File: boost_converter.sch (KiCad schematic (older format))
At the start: 9 parts, among them U4 TPS61236P

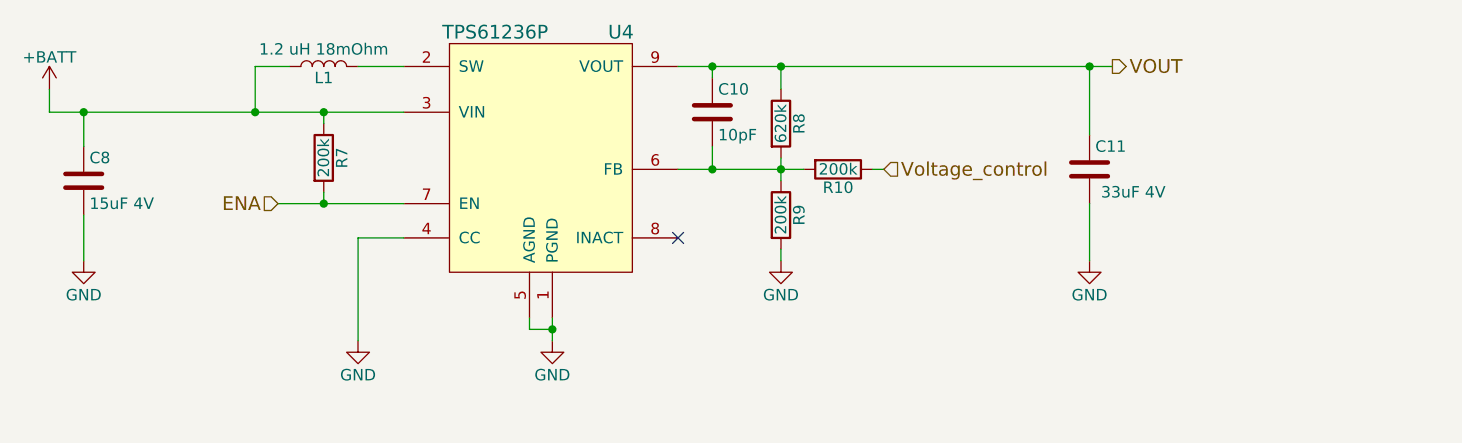
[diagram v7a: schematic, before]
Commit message: Changed pinout, added voltage and current reading
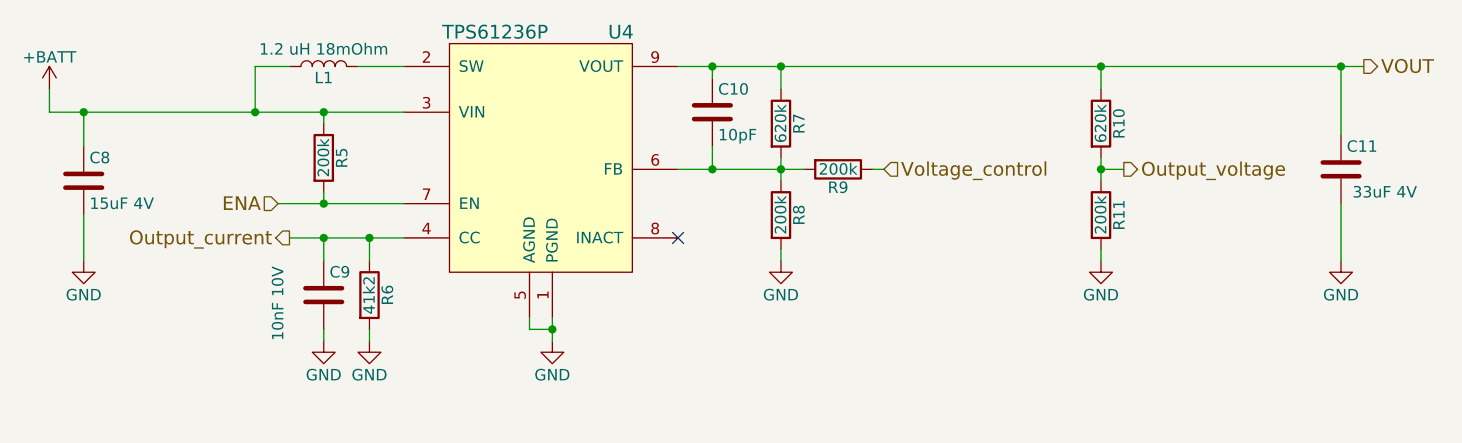
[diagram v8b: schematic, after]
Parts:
- added C9: 10nF 10V, Capacitors_SMD:C_0402, symbol C
- added R10: 620k, Resistors_SMD:R_0402, symbol R
- added R11: 200k, Resistors_SMD:R_0402, symbol R
- added R6: 41k2, Resistors_SMD:R_0402, symbol R
- C10: footprint (none) -> Capacitors_SMD:C_0402
- renumbered R7 to R5, R8 to R7, R9 to R8, R10 to R9
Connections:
- net GND: now also C9.2, R11.2, R6.2; no longer U4.4 (CC)
- net VOUT: now also R10.1
- new net Output_current: C9.1, R6.1, U4.4 (CC)
- new net Output_voltage: R10.2, R11.1
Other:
- moved on the sheet: C11
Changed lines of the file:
@@
 F 0 "C10" H 6575 3650 50  0000 L CNN
 F 1 "10pF" H 6575 3450 50  0000 L CNN
-F 2 "" H 6588 3400 50  0001 C CNN
+F 2 "Capacitors_SMD:C_0402" H 6588 3400 50  0001 C CNN
 F 3 "" H 6550 3550 50  0001 C CNN
 	1    6550 3550
@@
 $EndComp
 $Comp
-L R R8
+L R R7
 U 1 1 5AA40DAF
 P 6850 3600
-F 0 "R8" V 6930 3600 50  0000 C CNN
+F 0 "R7" V 6930 3600 50  0000 C CNN
 F 1 "620k" V 6850 3600 50  0000 C CNN
 F 2 "Resistors_SMD:R_0402" V 6780 3600 50  0001 C CNN
@@
 $EndComp
 $Comp
-L R R9
+L R R8
 U 1 1 5AA40DF4
 P 6850 4000
-F 0 "R9" V 6930 4000 50  0000 C CNN
+F 0 "R8" V 6930 4000 50  0000 C CNN
 F 1 "200k" V 6850 4000 50  0000 C CNN
 F 2 "Resistors_SMD:R_0402" V 6780 4000 50  0001 C CNN
@@
 $EndComp
 $Comp
-L GND #PWR032
+L GND #PWR37
 U 1 1 5AA40E28
 P 6850 4200
-F 0 "#PWR032" H 6850 3950 50  0001 C CNN
+F 0 "#PWR37" H 6850 3950 50  0001 C CNN
 F 1 "GND" H 6850 4050 50  0000 C CNN
 F 2 "" H 6850 4200 50  0001 C CNN
@@
 $EndComp
 $Comp
-L GND #PWR033
+L GND #PWR36
 U 1 1 5AA40E49
 P 5850 4550
-F 0 "#PWR033" H 5850 4300 50  0001 C CNN
+F 0 "#PWR36" H 5850 4300 50  0001 C CNN
 F 1 "GND" H 5850 4400 50  0000 C CNN
 F 2 "" H 5850 4550 50  0001 C CNN
@@
 L C C11
 U 1 1 5AA40FA0
-P 8200 3800
-F 0 "C11" H 8225 3900 50  0000 L CNN
-F 1 "33uF 4V" H 8250 3700 50  0000 L CNN
-F 2 "" H 8238 3650 50  0001 C CNN
-F 3 "" H 8200 3800 50  0001 C CNN
-F 4 "GRM21BR60G336ME15L" H 8200 3800 60  0001 C CNN "MPN"
-	1    8200 3800
-	1    0    0    -1
-$EndComp
-$Comp
-L GND #PWR034
+P 9300 3800
+F 0 "C11" H 9325 3900 50  0000 L CNN
+F 1 "33uF 4V" H 9350 3700 50  0000 L CNN
+F 2 "" H 9338 3650 50  0001 C CNN
+F 3 "" H 9300 3800 50  0001 C CNN
+F 4 "GRM21BR60G336ME15L" H 9300 3800 60  0001 C CNN "MPN"
+	1    9300 3800
+	1    0    0    -1
+$EndComp
+$Comp
+L GND #PWR39
 U 1 1 5AA40FE1
-P 8200 4200
-F 0 "#PWR034" H 8200 3950 50  0001 C CNN
-F 1 "GND" H 8200 4050 50  0000 C CNN
-F 2 "" H 8200 4200 50  0001 C CNN
-F 3 "" H 8200 4200 50  0001 C CNN
-	1    8200 4200
-	1    0    0    -1
-$EndComp
-Text HLabel 8300 3350 2    60   Output ~ 0
+P 9300 4200
+F 0 "#PWR39" H 9300 3950 50  0001 C CNN
+F 1 "GND" H 9300 4050 50  0000 C CNN
+F 2 "" H 9300 4200 50  0001 C CNN
+F 3 "" H 9300 4200 50  0001 C CNN
+	1    9300 4200
+	1    0    0    -1
+$EndComp
+Text HLabel 9400 3350 2    60   Output ~ 0
 VOUT
 $Comp
@@
 $EndComp
 $Comp
-L GND #PWR035
+L GND #PWR33
 U 1 1 5AA412DC
 P 3800 4200
-F 0 "#PWR035" H 3800 3950 50  0001 C CNN
+F 0 "#PWR33" H 3800 3950 50  0001 C CNN
 F 1 "GND" H 3800 4050 50  0000 C CNN
 F 2 "" H 3800 4200 50  0001 C CNN
@@
 $EndComp
 $Comp
-L R R7
+L R R5
 U 1 1 5AA417A7
 P 4850 3750
-F 0 "R7" V 4930 3750 50  0000 C CNN
+F 0 "R5" V 4930 3750 50  0000 C CNN
 F 1 "200k" V 4850 3750 50  0000 C CNN
 F 2 "Resistors_SMD:R_0402" V 4780 3750 50  0001 C CNN
@@
 	1    0    0    -1
 $EndComp
-Wire Wire Line
-	5850 4450 5850 4550
-Wire Wire Line
-	5750 4450 5750 4500
-Wire Wire Line
-	5750 4500 5850 4500
-Connection ~ 5850 4500
-Wire Wire Line
-	6850 4150 6850 4200
-Wire Wire Line
-	6850 3750 6850 3850
-Wire Wire Line
-	6850 3350 6850 3450
-Wire Wire Line
-	6400 3350 8300 3350
-Connection ~ 6850 3800
-Wire Wire Line
-	6550 3700 6550 3800
-Connection ~ 6550 3800
-Wire Wire Line
-	6550 3400 6550 3350
-Connection ~ 6550 3350
-Wire Wire Line
-	8200 3350 8200 3650
-Connection ~ 6850 3350
-Wire Wire Line
-	8200 3950 8200 4200
-Connection ~ 8200 3350
-Wire Wire Line
-	3650 3550 5200 3550
-Wire Wire Line
-	3800 3550 3800 3700
-Wire Wire Line
-	3800 4000 3800 4200
-Wire Wire Line
-	5200 3350 5000 3350
-Wire Wire Line
-	4700 3350 4550 3350
-Wire Wire Line
-	4550 3350 4550 3550
-Connection ~ 4550 3550
-Wire Wire Line
-	4850 3600 4850 3550
-Connection ~ 4850 3550
-Wire Wire Line
-	4850 3900 4850 3950
-Wire Wire Line
-	4650 3950 5200 3950
-$Comp
-L R R10
+$Comp
+L R R9
 U 1 1 5AA41C36
 P 7100 3800
-F 0 "R10" V 7180 3800 50  0000 C CNN
+F 0 "R9" V 7180 3800 50  0000 C CNN
 F 1 "200k" V 7100 3800 50  0000 C CNN
 F 2 "Resistors_SMD:R_0402" V 7030 3800 50  0001 C CNN
@@
 	0    1    1    0
 $EndComp
-Wire Wire Line
-	6400 3800 6950 3800
 Text HLabel 7300 3800 2    60   Input ~ 0
 Voltage_control
-Wire Wire Line
-	7250 3800 7300 3800
 Text HLabel 4650 3950 0    60   Input ~ 0
 ENA
-Connection ~ 4850 3950
-$Comp
-L +BATT #PWR036
+$Comp
+L +BATT #PWR32
 U 1 1 5AA423A0
 P 3650 3450
-F 0 "#PWR036" H 3650 3300 50  0001 C CNN
+F 0 "#PWR32" H 3650 3300 50  0001 C CNN
 F 1 "+BATT" H 3650 3590 50  0000 C CNN
 F 2 "" H 3650 3450 50  0001 C CNN
@@
 	1    0    0    -1
 $EndComp
+$Comp
+L R R10
+U 1 1 5AB62A62
+P 8250 3600
+F 0 "R10" V 8330 3600 50  0000 C CNN
+F 1 "620k" V 8250 3600 50  0000 C CNN
+F 2 "Resistors_SMD:R_0402" V 8180 3600 50  0001 C CNN
+F 3 "" H 8250 3600 50  0001 C CNN
+	1    8250 3600
+	1    0    0    -1
+$EndComp
+$Comp
+L R R11
+U 1 1 5AB62B12
+P 8250 4000
+F 0 "R11" V 8330 4000 50  0000 C CNN
+F 1 "200k" V 8250 4000 50  0000 C CNN
+F 2 "Resistors_SMD:R_0402" V 8180 4000 50  0001 C CNN
+F 3 "" H 8250 4000 50  0001 C CNN
+	1    8250 4000
+	1    0    0    -1
+$EndComp
+$Comp
+L GND #PWR38
+U 1 1 5AB62B99
+P 8250 4200
+F 0 "#PWR38" H 8250 3950 50  0001 C CNN
+F 1 "GND" H 8250 4050 50  0000 C CNN
+F 2 "" H 8250 4200 50  0001 C CNN
+F 3 "" H 8250 4200 50  0001 C CNN
+	1    8250 4200
+	1    0    0    -1
+$EndComp
+Wire Wire Line
+	5850 4450 5850 4550
+Wire Wire Line
+	5750 4450 5750 4500
+Wire Wire Line
+	5750 4500 5850 4500
+Connection ~ 5850 4500
+Wire Wire Line
+	6850 4150 6850 4200
+Wire Wire Line
+	6850 3750 6850 3850
+Wire Wire Line
+	6850 3350 6850 3450
+Wire Wire Line
+	6400 3350 9400 3350
+Connection ~ 6850 3800
+Wire Wire Line
+	6550 3700 6550 3800
+Connection ~ 6550 3800
+Wire Wire Line
+	6550 3400 6550 3350
+Connection ~ 6550 3350
+Wire Wire Line
+	9300 3350 9300 3650
+Connection ~ 6850 3350
+Wire Wire Line
+	9300 3950 9300 4200
+Connection ~ 9300 3350
+Wire Wire Line
+	3650 3550 5200 3550
+Wire Wire Line
+	3800 3550 3800 3700
+Wire Wire Line
+	3800 4000 3800 4200
+Wire Wire Line
+	5200 3350 5000 3350
+Wire Wire Line
+	4700 3350 4550 3350
+Wire Wire Line
+	4550 3350 4550 3550
+Connection ~ 4550 3550
+Wire Wire Line
+	4850 3600 4850 3550
+Connection ~ 4850 3550
+Wire Wire Line
+	4850 3900 4850 3950
+Wire Wire Line
+	4650 3950 5200 3950
+Wire Wire Line
+	6400 3800 6950 3800
+Wire Wire Line
+	7250 3800 7300 3800
+Connection ~ 4850 3950
 Wire Wire Line
 	3650 3450 3650 3550
 Connection ~ 3800 3550
-$Comp
-L GND #PWR037
-U 1 1 5AA42711
-P 5000 4550
-F 0 "#PWR037" H 5000 4300 50  0001 C CNN
-F 1 "GND" H 5000 4400 50  0000 C CNN
-F 2 "" H 5000 4550 50  0001 C CNN
-F 3 "" H 5000 4550 50  0001 C CNN
-	1    5000 4550
-	1    0    0    -1
-$EndComp
-Wire Wire Line
-	5000 4100 5000 4550
-Wire Wire Line
-	5200 4100 5000 4100
+Wire Wire Line
+	8250 3450 8250 3350
+Connection ~ 8250 3350
+Wire Wire Line
+	8250 3750 8250 3850
+Wire Wire Line
+	8250 4150 8250 4200
+Text HLabel 8350 3800 2    60   Output ~ 0
+Output_voltage
+Wire Wire Line
+	8350 3800 8250 3800
+Connection ~ 8250 3800
+Text HLabel 4700 4100 0    60   Output ~ 0
+Output_current
+$Comp
+L R R6
+U 1 1 5AB632FE
+P 5050 4350
+F 0 "R6" V 5130 4350 50  0000 C CNN
+F 1 "41k2" V 5050 4350 50  0000 C CNN
+F 2 "Resistors_SMD:R_0402" V 4980 4350 50  0001 C CNN
+F 3 "" H 5050 4350 50  0001 C CNN
+	1    5050 4350
+	1    0    0    -1
+$EndComp
+Wire Wire Line
+	4700 4100 5200 4100
+Wire Wire Line
+	5050 4100 5050 4200
+$Comp
+L GND #PWR35
+U 1 1 5AB63392
+P 5050 4550
+F 0 "#PWR35" H 5050 4300 50  0001 C CNN
+F 1 "GND" H 5050 4400 50  0000 C CNN
+F 2 "" H 5050 4550 50  0001 C CNN
+F 3 "" H 5050 4550 50  0001 C CNN
+	1    5050 4550
+	1    0    0    -1
+$EndComp
+Wire Wire Line
+	5050 4500 5050 4550
+$Comp
+L C C9
+U 1 1 5AB63412
+P 4850 4350
+F 0 "C9" H 4875 4450 50  0000 L CNN
+F 1 "10nF 10V" V 4650 4150 50  0000 L CNN
+F 2 "Capacitors_SMD:C_0402" H 4888 4200 50  0001 C CNN
+F 3 "" H 4850 4350 50  0001 C CNN
+	1    4850 4350
+	1    0    0    -1
+$EndComp
+Wire Wire Line
+	4850 4200 4850 4100
+Connection ~ 5050 4100
+$Comp
+L GND #PWR34
+U 1 1 5AB634B2
+P 4850 4550
+F 0 "#PWR34" H 4850 4300 50  0001 C CNN
+F 1 "GND" H 4850 4400 50  0000 C CNN
+F 2 "" H 4850 4550 50  0001 C CNN
+F 3 "" H 4850 4550 50  0001 C CNN
+	1    4850 4550
+	1    0    0    -1
+$EndComp
+Wire Wire Line
+	4850 4500 4850 4550
+Connection ~ 4850 4100
 $EndSCHEMATC
